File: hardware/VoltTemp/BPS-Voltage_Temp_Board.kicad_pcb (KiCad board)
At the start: 2 copper layers, 98.2 x 56.2 mm, 143 parts, among them IC1 ISO1641BDR, J10 53307-2471, J11 Conn_01x07, J12 Conn_01x04, J13 Conn_01x04, J5 Logic_Analyzer, J6 Conn_01x04, J7 Conn_01x04, J8 Conn_01x06, J9 Conn_01x03, SW1 BOOT, U1 EL3H7, U12 TLV9062xD, U13 TLV9062xD, U14 TLV9062xD, U2 BQ7692003PW, U3 EL3H7, U4 TLV9062xD, U6 TLV9062xD

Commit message: some ocd stuff
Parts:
- moved R59 1.10 mm to (168.0, 88.1)
- moved C24 0.96 mm to (167.8, 92.1)
- moved C4 0.35 mm to (170.5, 88.1)
- turned C34 to -90 degrees
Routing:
- net /LedDin: track 57.5 -> 109.1 mm, vias 1 -> 3
- net /VoltageConn/VC0: track 19.6 -> 25.1 mm
- net /VoltageConn/last_cell: track 3.66 -> 5.70 mm
- net Net-(C4-Pad1): track 3.94 -> 5.04 mm
- net GND: track 6.64 -> 6.84 mm, vias 34 -> 53
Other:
- board text added: "Todo: - Layout :( [] - Update constrains [] - Mirror thermistor flex pinout [] - Label voltage connector [] - Fix iso i2c footprint [X] - Make proper edge cuts [X] - Add stitching vias [] - Update pcb from schematic once schematic todo done [X] - Figure out edge to connector clearance for nanofits [] - Redo addressable led routing [] - Verify 24V traces can handle 8 Volttemps of current [X] - Mak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"
- board text removed: "Todo: - Layout :( [] - Update constrains [] - Mirror thermistor flex pinout [] - Label voltage connector - Fix iso i2c footprint [X] - Make proper edge cuts [X] - Add stitching vias [] - Update pcb from schematic once schematic todo done [] - Figure out edge to connector clearance for nanofits [] - Redo addressable led routing [] - Verify 24V traces can handle 8 Volttemps of current [X] - Make si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"

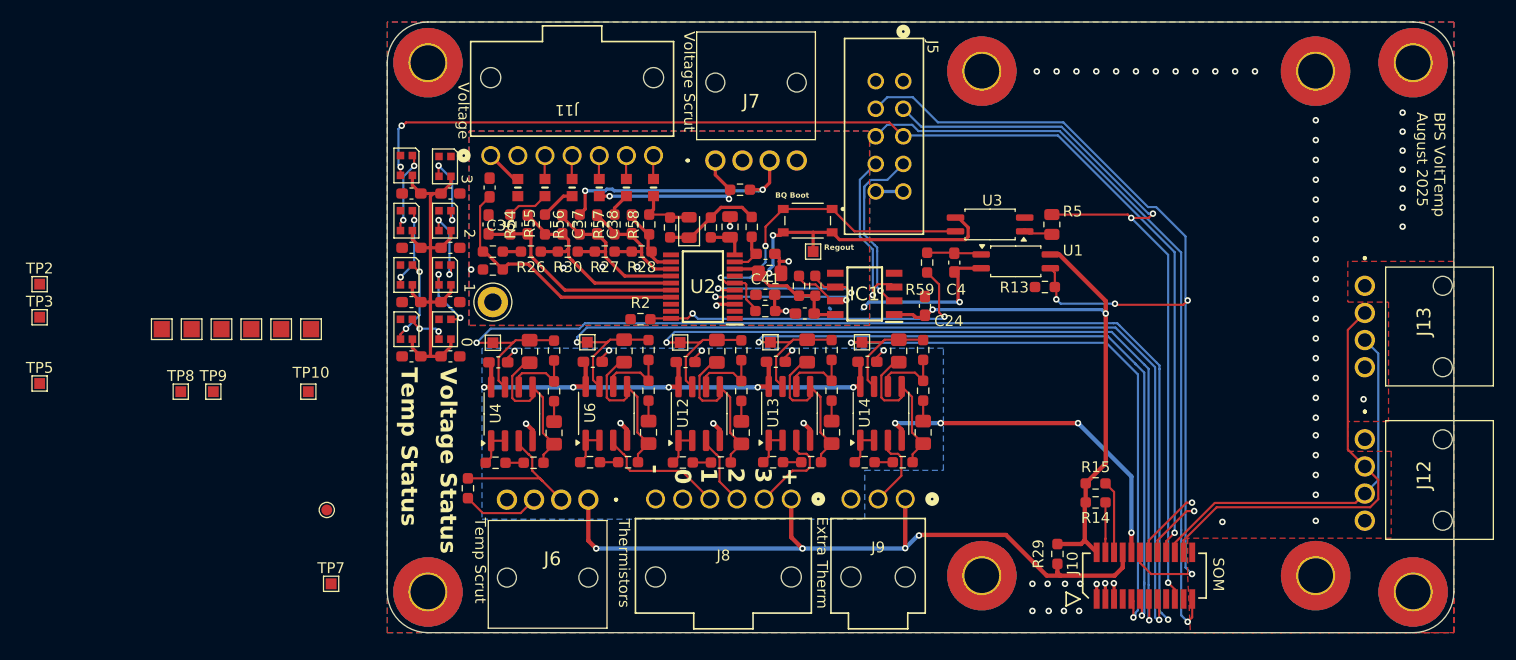
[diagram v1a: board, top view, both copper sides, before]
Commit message: add thermistor test board, just need to route volttemp testpoints
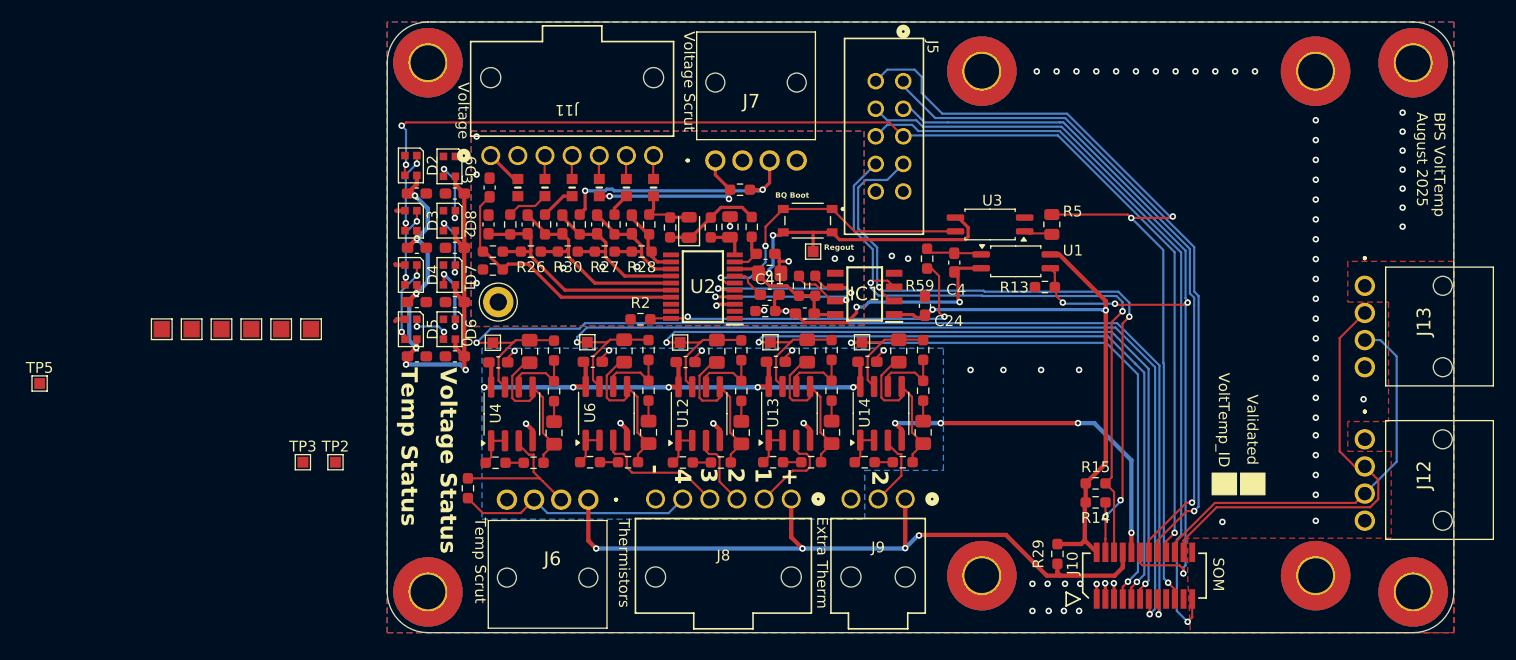
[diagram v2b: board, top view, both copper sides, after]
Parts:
- removed TP10, TP7, TP8, TP9: TP_TempIn, TestPoint:TestPoint_Pad_1.0x1.0mm
- removed TP6: TP_TempIn, TestPoint:TestPoint_Pad_D1.0mm
- D2, D3, D4, D5, D6, D7, D8, D9: footprint LED_SMD:LED_WS2812B-2020_PLCC4_2.0x2.0mm -> VoltTemp:WS2812B-2020
- MH1, MH2, MH3, MH4: value M3 -> MountingHole_Pad
- moved TP2 31.8 mm to (113.5, 106.5)
- moved TP3 27.7 mm to (110.5, 106.5)
- moved C10 0.50 mm to (121.0, 81.8), turned to 0 degrees
- moved C11 0.50 mm to (121.0, 86.8), turned to 0 degrees
- moved C12 0.50 mm to (121.0, 91.8), turned to 0 degrees
- moved C13 0.50 mm to (121.0, 96.8), turned to 0 degrees
- moved TP4 0.50 mm to (128.5, 91.8)
- moved C14 0.41 mm to (124.5, 96.8), turned to 180 degrees
- moved C15 0.41 mm to (124.5, 91.8), turned to 180 degrees
- moved C16 0.41 mm to (124.5, 86.8), turned to 180 degrees
- moved C17 0.41 mm to (124.5, 81.8), turned to 180 degrees
- moved D2 0.41 mm to (120.5, 79.2)
- moved D3 0.41 mm to (120.5, 84.2)
- moved D4 0.41 mm to (120.5, 89.2)
- moved D5 0.41 mm to (120.5, 94.2)
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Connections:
- net /TemperatureConn/rawTemperature0_Pre renamed /TemperatureConn/rawTemperature4_Pre
- C18 pad 2: GND2 -> GND_Seg
- C2 pad 1: GND2 -> GND_Seg
- C25 pad 2: /TemperatureFilters/Temperature0 -> /TemperatureFilters/Temperature4
- C27 pad 2: /TemperatureFilters/Temperature1 -> /TemperatureFilters/Temperature3
- C31 pad 2: /TemperatureFilters/Temperature3 -> /TemperatureFilters/Temperature1
- C33 pad 2: /TemperatureFilters/Temperature4 -> /TemperatureFilters/Temperature5
- C34 pad 1: GND2 -> GND_Seg
- C35 pad 2: GND2 -> GND_Seg
- C4 pad 2: GND2 -> GND_Seg
- C40 pad 2: GND2 -> GND_Seg
- C41 pad 2: GND2 -> GND_Seg
- C42 pad 2: GND2 -> GND_Seg
- IC1 pad 5: GND2 -> GND_Seg
- J10 pad 11: /TemperatureFilters/Temperature3 -> /TemperatureFilters/Temperature2
- J10 pad 13: /TemperatureFilters/Temperature2 -> /TemperatureFilters/Temperature3
- J10 pad 15: /TemperatureFilters/Temperature1 -> /TemperatureFilters/Temperature4
- J10 pad 7: /TemperatureFilters/Temperature0 -> /TemperatureFilters/Temperature5
- J10 pad 9: /TemperatureFilters/Temperature4 -> /TemperatureFilters/Temperature1
- J5 pad 2: /PB14 -> /bmsEn
- J5 pad 3: /bmsEn -> /PB14
- J6 pad 2: /TemperatureConn/rawTemperature0 -> /TemperatureConn/rawTemperature4
- J7 pad 4: GND2 -> GND_Seg
- J8 pad 2: /TemperatureConn/rawTemperature3 -> /TemperatureConn/rawTemperature1
- J8 pad 4: /TemperatureConn/rawTemperature1 -> /TemperatureConn/rawTemperature3
- J9 pad 2: /TemperatureConn/rawTemperature4 -> /TemperatureConn/rawTemperature5
- MH1 pad 1: (no net) -> unconnected-(MH1-Pad1)_2
- MH2 pad 1: (no net) -> unconnected-(MH2-Pad1)_2
- MH3 pad 1: (no net) -> unconnected-(MH3-Pad1)_2
- MH4 pad 1: (no net) -> unconnected-(MH4-Pad1)
- R11 pad 1: GND2 -> GND_Seg
- R2 pad 2: GND2 -> GND_Seg
- R24 pad 1: /TemperatureConn/rawTemperature0 -> /TemperatureConn/rawTemperature4
- R36 pad 2: /TemperatureFilters/Temperature0 -> /TemperatureFilters/Temperature4
- R40 pad 2: /TemperatureFilters/Temperature1 -> /TemperatureFilters/Temperature3
- R48 pad 2: /TemperatureFilters/Temperature3 -> /TemperatureFilters/Temperature1
- R52 pad 2: /TemperatureFilters/Temperature4 -> /TemperatureFilters/Temperature5
- R53 pad 2: GND2 -> GND_Seg
- TP11 pad 1: /TemperatureFilters/Temperature0 -> /TemperatureFilters/Temperature4
- TP12 pad 1: /TemperatureFilters/Temperature1 -> /TemperatureFilters/Temperature3
- TP14 pad 1: /TemperatureFilters/Temperature3 -> /TemperatureFilters/Temperature1
- TP15 pad 1: /TemperatureFilters/Temperature4 -> /TemperatureFilters/Temperature5
- TP4 pad 1: GND2 -> GND_Seg
- U1 pad 2: GND2 -> GND_Seg
- U13 pad 3: /TemperatureConn/rawTemperature3 -> /TemperatureConn/rawTemperature1
- U13 pad 7: /TemperatureFilters/Temperature3 -> /TemperatureFilters/Temperature1
- U14 pad 3: /TemperatureConn/rawTemperature4 -> /TemperatureConn/rawTemperature5
- U14 pad 7: /TemperatureFilters/Temperature4 -> /TemperatureFilters/Temperature5
- U2 pad 18: GND2 -> GND_Seg
- U2 pad 19: GND2 -> GND_Seg
- U2 pad 3: GND2 -> GND_Seg
- U4 pad 3: /TemperatureConn/rawTemperature0 -> /TemperatureConn/rawTemperature4
- U4 pad 7: /TemperatureFilters/Temperature0 -> /TemperatureFilters/Temperature4
- U6 pad 3: /TemperatureConn/rawTemperature1 -> /TemperatureConn/rawTemperature3
- U6 pad 7: /TemperatureFilters/Temperature1 -> /TemperatureFilters/Temperature3
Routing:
- net /TemperatureFilters/Temperature0: track 101.2 -> 0.00 mm, vias 2 -> 0
- net /TemperatureFilters/Temperature5: track 0.00 -> 60.6 mm, vias 0 -> 2
- net /PB15: track 5.60 -> 63.6 mm
- net /PB14: track 6.52 -> 61.9 mm
- net /VoltageSense/I2C_SDA: track 21.9 -> 65.9 mm, vias 1 -> 4
- net /VoltageSense/I2C_SCL: track 22.7 -> 63.3 mm, vias 1 -> 2
- net /TemperatureFilters/Temperature4: track 63.7 -> 102.2 mm
- net GND_Seg: track 0.00 -> 30.8 mm, vias 0 -> 14
- net GND2: track 23.6 -> 0.00 mm, vias 10 -> 0
- net /TemperatureFilters/Temperature1: track 92.8 -> 70.7 mm
- net /TemperatureFilters/Temperature3: track 73.4 -> 91.7 mm
- net +3V3: track 38.4 -> 55.4 mm, vias 0 -> 6
- net /TemperatureConn/rawTemperature4_Pre: track 7.62 -> 22.4 mm
- net /TemperatureConn/rawTemperature0: track 14.5 -> 0.00 mm
- net /bmsEn: track 73.4 -> 82.4 mm
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- added copper zone on B.Cu, net GND_Seg
- added copper zone on F.Cu, net GND_Seg
- removed copper zone on B.Cu, net GND2
- removed copper zone on F.Cu, net GND2
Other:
- board text added: "4"
- board text added: "Todo: - Layout :( [] - Update constrains [X] - Mirror thermistor flex pinout [X] - Label voltage connector [] - Fix iso i2c footprint [X] - Make proper edge cuts [X] - Add stitching vias [] - Update pcb from schematic once schematic todo done [X] - Figure out edge to connector clearance for nanofits [] - Redo addressable led routing [] - Verify 24V traces can handle 8 Volttemps of current [X] - M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"
- board text added: "Validated"
- board text added: "VoltTemp_ID"
- board text removed: "Todo: - Layout :( [] - Update constrains [] - Mirror thermistor flex pinout [] - Label voltage connector [] - Fix iso i2c footprint [X] - Make proper edge cuts [X] - Add stitching vias [] - Update pcb from schematic once schematic todo done [X] - Figure out edge to connector clearance for nanofits [] - Redo addressable led routing [] - Verify 24V traces can handle 8 Volttemps of current [X] - Mak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"

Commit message: redid thermistor board
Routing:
- net /VoltageSense/bmsBoot: track 29.3 -> 28.5 mm, vias 3 -> 2
- net /TemperatureConn/rawTemperature4: track 14.4 -> 13.9 mm
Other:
- board text added: "Segment -"
- board text removed: "0"
